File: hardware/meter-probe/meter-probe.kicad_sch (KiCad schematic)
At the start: 37 parts, among them J1 Cable, J2 Cable, SW1 Sensor Button, U1 TSL2585, U2 M24C02-D, U3 PCA9527, U4 TC1301A-APA, U5 USBLC6-2SC6

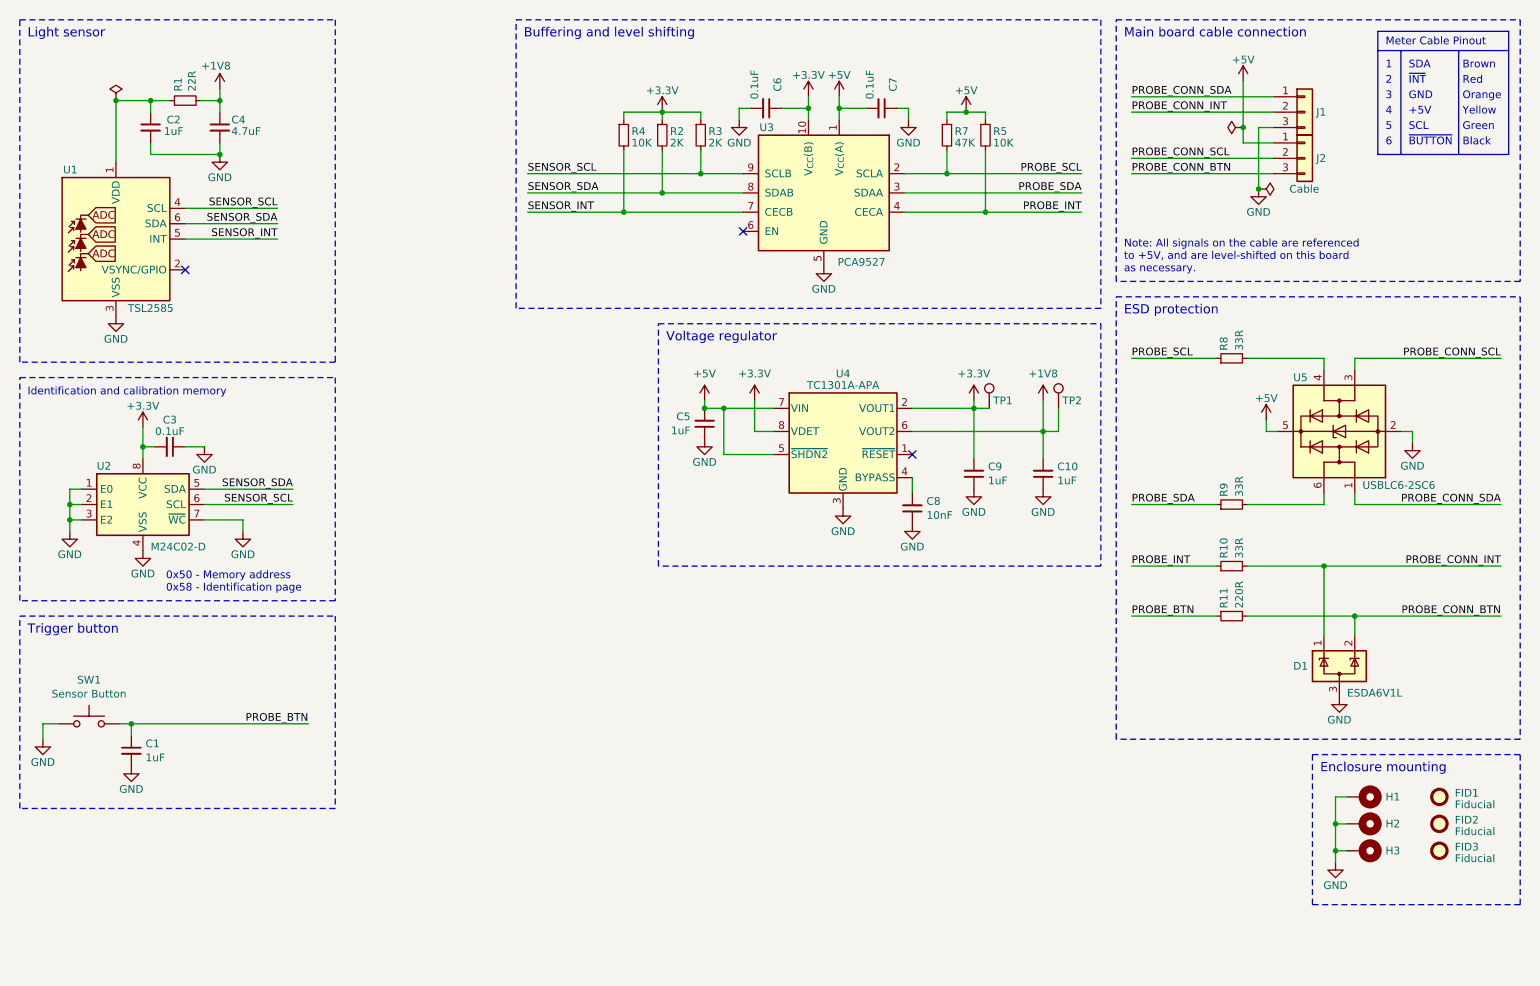
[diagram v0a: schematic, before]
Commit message: Update meter probe with a variety of changes based on testing and eval
- Add a TCA9801 I2C buffer to remove the static offset induced by the
  PCA9527 and provide a clean 1.8V I2C signal to the sensor.
  While the board does work fine without this, the 0.5V static offset
  from the PCA9527 is too close for comfort to the sensor's 0.54V low
  level. So this is a proactive change to reduce potential issues later.
- Add a small series resistor to the push button, to limit the current
  across the debounce capacitor when the button is pressed.
- Add a series of test points at the board edge, so a pogo pin test clip
  can be used more easily to verify board operation prior to attachment
  of the interfae cable.
- Increase board length by 1mm to accomodate the test points.
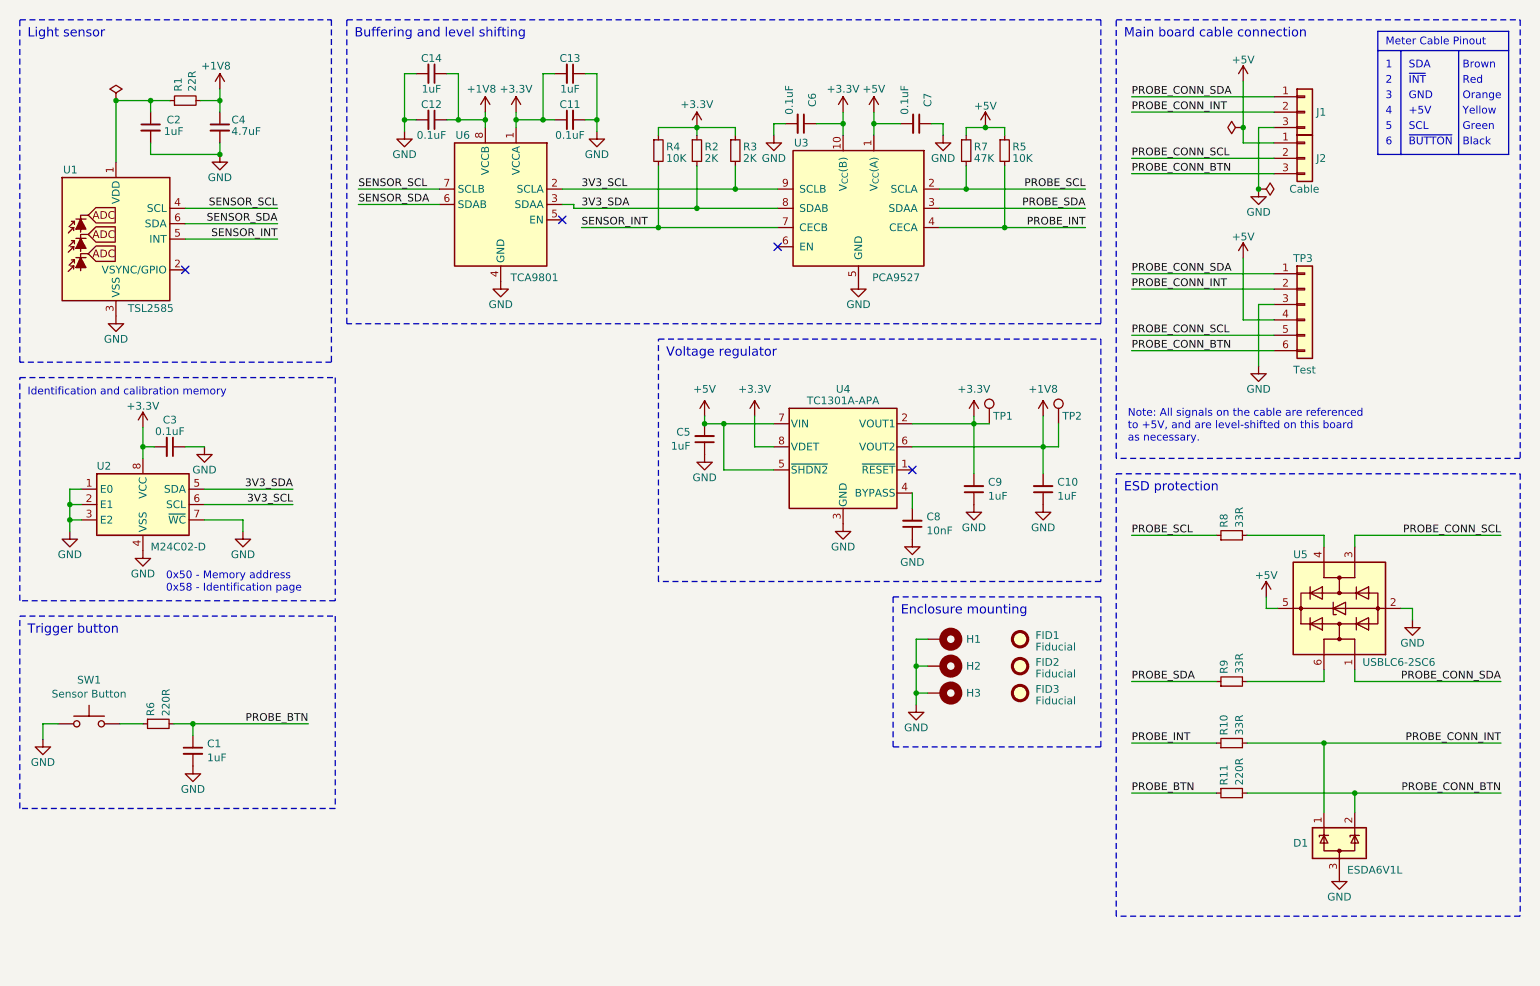
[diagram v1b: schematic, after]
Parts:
- added C11, C12: 0.1uF, Capacitor_SMD:C_0603_1608Metric, symbol Device:C_Small
- added C13, C14: 1uF, Capacitor_SMD:C_0603_1608Metric, symbol Device:C_Small
- added R6: 220R, Resistor_SMD:R_0603_1608Metric, symbol Device:R_Small
- added TP3: Test, lib_fp:TestPoint_1x06_P2.54mm, symbol Connector_Generic:Conn_01x06
- added U6: TCA9801, Package_SO:VSSOP-8_3.0x3.0mm_P0.65mm, symbol Interface:TCA9801
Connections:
- net +1V8: now also C12.1, C14.1, U6.8 (VCCB)
- net +3.3V: now also C11.1, C13.2, U6.1 (VCCA)
- net +5V: now also TP3.4 (Pin_4)
- net GND: now also C11.2, C12.2, C13.1, C14.2, TP3.3 (Pin_3), U6.4 (GND)
- net PROBE_BTN: now also R6.2; no longer SW1.2
- net PROBE_CONN_BTN: now also TP3.6 (Pin_6)
- net PROBE_CONN_INT: now also TP3.2 (Pin_2)
- net PROBE_CONN_SCL: now also TP3.5 (Pin_5)
- net PROBE_CONN_SDA: now also TP3.1 (Pin_1)
- net SENSOR_SCL: now also U6.7 (SCLB); no longer R3.2, U2.6 (SCL), U3.9 (SCLB)
- net SENSOR_SDA: now also U6.6 (SDAB); no longer R2.2, U2.5 (SDA), U3.8 (SDAB)
- new net: R6.1, SW1.2
- new net 3V3_SCL: R3.2, U2.6 (SCL), U3.9 (SCLB), U6.2 (SCLA)
- new net 3V3_SDA: R2.2, U2.5 (SDA), U3.8 (SDAB), U6.3 (SDAA)
- no-connect marks 3 -> 4
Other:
- moved on the sheet: C1, C10, C5, C6, C7, C8, C9, D1, FID1, FID2, FID3, H1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

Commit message: Initial implementation of FT260 in meter probe schematic
This is a big change towards using a USB interface for the meter probe,
and is the first step of getting the schematic portion put together.
Most of the designators will likely change after the layout is started.

The intent of this change is to leverage off-the-shelf mass produced mouse
cables for the physical connection, and to run the meter probe over a
protocol better suited to hot-plugging and noise immunity.
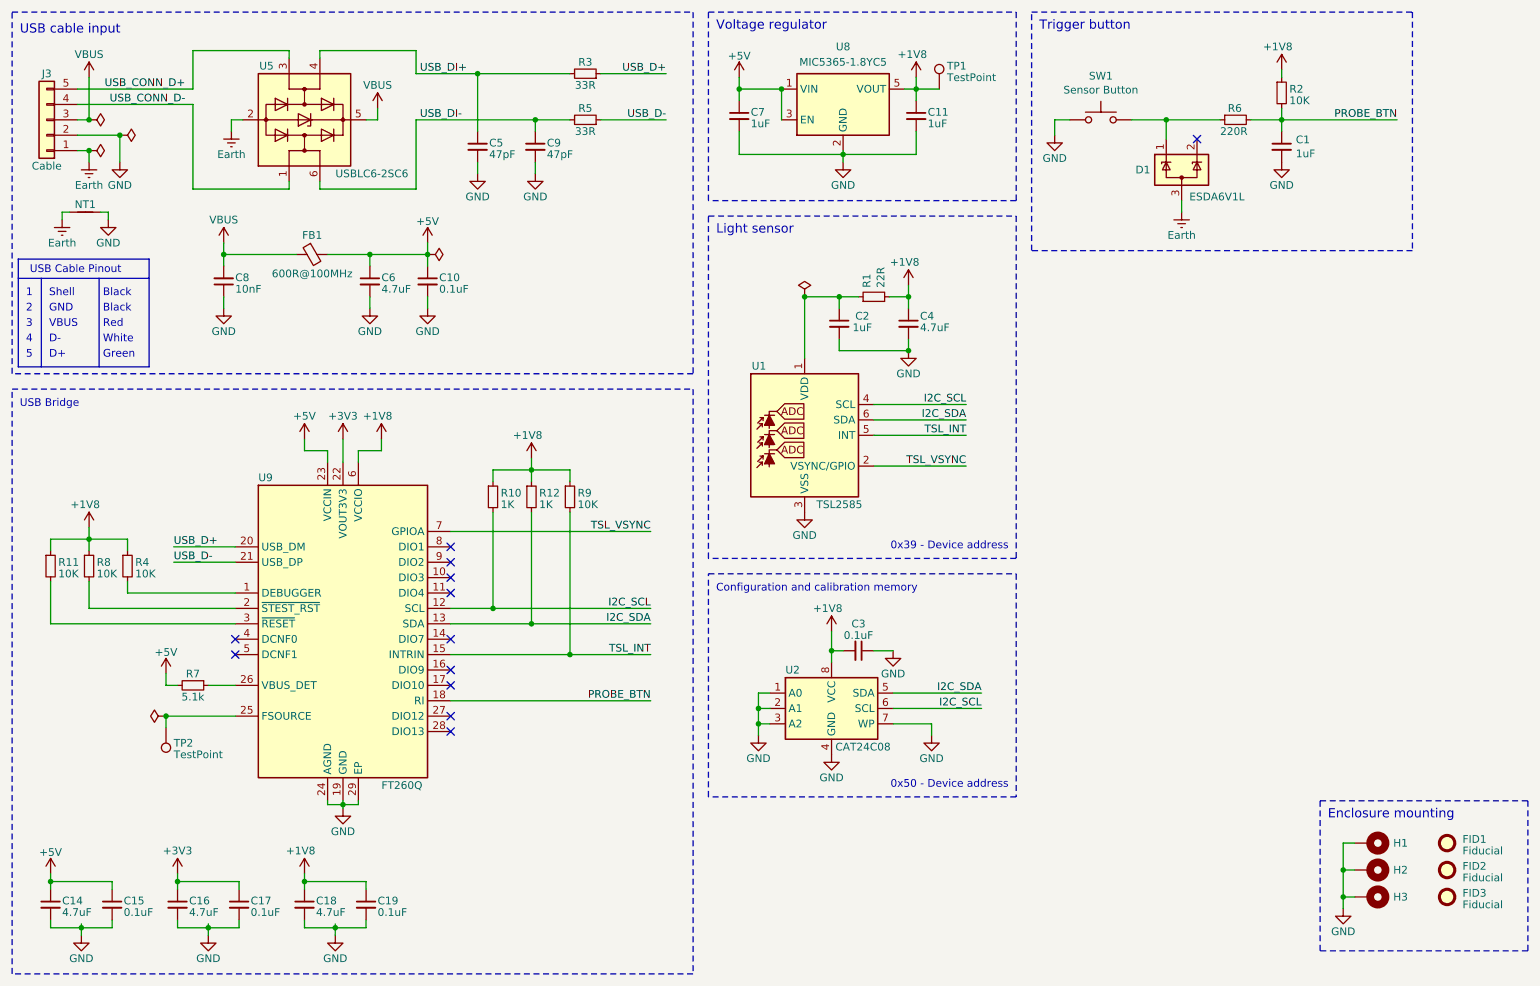
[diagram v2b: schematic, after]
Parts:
- removed C12: 0.1uF, Capacitor_SMD:C_0603_1608Metric, symbol Device:C_Small
- removed C13: 1uF, Capacitor_SMD:C_0603_1608Metric, symbol Device:C_Small
- removed J1, J2: Cable, lib_fp:AVX_IDC-009175-003-001, symbol Connector_Generic:Conn_01x03
- removed TP3: Test, lib_fp:TestPoint_1x06_P2.54mm, symbol Connector_Generic:Conn_01x06
- removed U2: M24C02-D, Package_SO:TSSOP-8_4.4x3mm_P0.65mm, symbol Memory_EEPROM:M24C02-RDW
- removed U3: PCA9527, Package_SO:TSSOP-10_3x3mm_P0.5mm, symbol Project:PCA9527
- removed U4: TC1301A-APA, Package_SO:MSOP-8_3x3mm_P0.65mm, symbol Project:TC1301A
- removed U6: TCA9801, Package_SO:VSSOP-8_3.0x3.0mm_P0.65mm, symbol Interface:TCA9801
- added C15, C17, C19: 0.1uF, Capacitor_SMD:C_0603_1608Metric, symbol Device:C_Small
- added C16, C18: 4.7uF, Capacitor_SMD:C_0603_1608Metric, symbol Device:C_Small
- added FB1: 600R@100MHz, Inductor_SMD:L_0603_1608Metric, symbol Device:FerriteBead_Small
- added J3: Cable, Connector_JST:JST_PH_B5B-PH-SM4-TB_1x05-1MP_P2.00mm_Vertical, symbol Connector_Generic:Conn_01x05
- added NT1: NetTie_2, NetTie:NetTie-2_SMD_Pad0.5mm, symbol Device:NetTie_2
- added R12: 1K, Resistor_SMD:R_0603_1608Metric, symbol Device:R_Small
- added U2: CAT24C08, Package_SO:SOIC-8_3.9x4.9mm_P1.27mm, symbol Project:CAT24C08
- added U8: MIC5365-1.8YC5, Package_TO_SOT_SMD:SOT-353_SC-70-5, symbol Regulator_Linear:MIC5365-3.3YC5
- added U9: FT260Q, lib_fp:FTDI_WQFN-28-1EP_5x5mm_P0.5mm_EP3.3x3.3mm, symbol Project:FT260Q
- C1: Supplier Digi-Key -> LCSC; Supplier PN 1276-1184-1-ND -> C29936
- C10: value 1uF -> 0.1uF; Manufacturer PN CL10B105KA8NNNC -> CL10B104KA8NNNC; Supplier LCSC -> Digi-Key; Supplier PN C29936 -> 1276-1006-1-ND
- C11, C7: value 0.1uF -> 1uF; Manufacturer PN CL10B104KA8NNNC -> CL10B105KA8NNNC; Supplier Digi-Key -> LCSC; Supplier PN 1276-1006-1-ND -> C29936
- C14: value 1uF -> 4.7uF; Manufacturer PN CL10B105KA8NNNC -> CL10A475KA8NQNC; Supplier PN C29936 -> C69335
- C5, C9: value 1uF -> 47pF; Manufacturer Samsung Electro-Mechanics -> YAGEO; Manufacturer PN CL10B105KA8NNNC -> CC0603JRNPO9BN470; Supplier LCSC -> Digi-Key; Supplier PN C29936 -> 311-1065-1-ND
- C6: value 0.1uF -> 4.7uF; Manufacturer PN CL10B104KA8NNNC -> CL10A475KA8NQNC; Supplier Digi-Key -> LCSC; Supplier PN 1276-1006-1-ND -> C69335
- C8: footprint Capacitor_SMD:C_0805_2012Metric -> Capacitor_SMD:C_0603_1608Metric; Manufacturer Samsung Electro-Mechanic -> YAGEO; Manufacturer PN CL21B103KBANNNC -> CC0603KRX7R8BB103; Supplier PN 1276-1015-1-ND -> 311-1360-1-ND
- R10: value 33R -> 1K; Manufacturer YAGEO -> Vishay Dale; Manufacturer PN RC0603JR-0733RL -> CRCW06031K00JNEA; Supplier PN 311-33GRCT-ND -> 541-1.0KGCT-ND
- R11: value 220R -> 10K; Manufacturer YAGEO -> Vishay Dale; Manufacturer PN RC0603JR-07220RL -> CRCW060310K0JNEA; Supplier PN 311-220GRCT-ND -> 541-10KGCT-ND
- R2: value 2K -> 10K; Manufacturer PN CRCW06032K00JNEA -> CRCW060310K0JNEA; Supplier PN 541-2.0KGCT-ND -> 541-10KGCT-ND
- R3: value 2K -> 33R; Manufacturer Vishay Dale -> YAGEO; Manufacturer PN CRCW06032K00JNEA -> RC0603JR-0733RL; Supplier PN 541-2.0KGCT-ND -> 311-33GRCT-ND
- R5: value 10K -> 33R; Manufacturer Vishay Dale -> YAGEO; Manufacturer PN CRCW060310K0JNEA -> RC0603JR-0733RL; Supplier PN 541-10KGCT-ND -> 311-33GRCT-ND
- R7: value 47K -> 5.1k; Manufacturer Vishay Dale -> Yaego; Manufacturer PN CRCW060347K0JNEA -> RC0603JR-075K1L; Supplier Digi-Key -> LCSC; Supplier PN 541-47KGCT-ND -> C14677
- R8, R9: value 33R -> 10K; Manufacturer YAGEO -> Vishay Dale; Manufacturer PN RC0603JR-0733RL -> CRCW060310K0JNEA; Supplier PN 311-33GRCT-ND -> 541-10KGCT-ND
- TP1: value 3.3V -> TestPoint; footprint TestPoint:TestPoint_Pad_D2.0mm -> TestPoint:TestPoint_Pad_D1.0mm; User Label 3.3V -> (none)
- TP2: value 1.8V -> TestPoint; footprint TestPoint:TestPoint_Pad_D2.0mm -> TestPoint:TestPoint_Pad_D1.0mm; User Label 3.3V -> (none)
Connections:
- net 3V3_SDA is gone; now on net PROBE_BTN: R2.2
- net PROBE_SDA is gone; now on net +1V8: R9.1
- net SENSOR_SCL is gone; now on net I2C_SCL: U1.4 (SCL)
- net +1V8: now also C11.1, C3.2, R10.1, R11.1, R2.1, R4.1, R8.1, TP1.1, C18.1, C19.1, R12.1, U2.8 (VCC), U8.5 (VOUT), U9.6 (VCCIO); no longer C10.2, C14.1, TP2.1
- net +5V: now also C10.1, C14.1, C6.1, C7.1, R7.2, C15.1, FB1.2, U8.1 (VIN), U8.3 (EN), U9.23 (VCCIN); no longer C5.2, C7.2, R5.1, R7.1, U5.5 (VBUS)
- net GND: now also C10.2, C5.2, C7.2, C9.2, C15.2, C16.2, C17.2, C18.2, C19.2, J3.2 (Pin_2), NT1.1, U2.1 (A0), U2.2 (A1), U2.3 (A2), U2.4 (GND), U2.7 (WP), U8.2 (GND), U9.19 (GND), U9.24 (AGND), U9.29 (EP); no longer C10.1, C5.1, C7.1, C9.1, D1.3 (A), U5.2 (GND)
- net PROBE_BTN: now also U9.18 (DIO11); no longer R11.1
- net at R6.1, SW1.2: now also D1.1 (K)
- net at R8.2: now also U9.2 (~{STEST_RST}); no longer U5.4 (I/O2)
- net TSL_INT: now reaches R9.2
- net TSL_INT: now also U1.5 (INT), U9.15 (DIO8); no longer U5.6 (I/O1)
- net VBUS: now reaches C8.2
- net VBUS: now also U5.5 (VBUS), FB1.1, J3.3 (Pin_3)
- net TSL_VSYNC: now reaches U1.2 (VSYNC/GPIO)
- net TSL_VSYNC: now also U9.7 (DIO0)
- removed net +3.3V: C11.1, C3.2, C6.1, C9.2, R2.1, R3.1, R4.1, TP1.1
- net 3V3_SCL renamed USB_DI+
- net USB_DI+: now also C5.1, U5.4 (I/O2)
- net PROBE_CONN_BTN: no longer names the net of R11.2
- net PROBE_CONN_BTN: now also U9.3 (~{RESET}); no longer D1.2 (K)
- net PROBE_CONN_INT renamed I2C_SCL
- net I2C_SCL: now also U2.6 (SCL), U9.12 (DIO5); no longer D1.1 (K)
- net PROBE_CONN_SCL renamed USB_CONN_D+
- net USB_CONN_D+: now also J3.5 (Pin_5)
- net PROBE_CONN_SDA renamed USB_CONN_D-
- net USB_CONN_D-: now also J3.4 (Pin_4)
- net PROBE_INT renamed USB_DI-
- net USB_DI-: now also C9.1, U5.6 (I/O1); no longer R10.1
- removed net PROBE_SCL: R7.2, R8.1
- net SENSOR_INT: no longer names the net of R4.2
- net SENSOR_INT: now also U9.1 (DEBUGGER); no longer U1.5 (INT)
- net SENSOR_SDA renamed I2C_SDA
- net I2C_SDA: now also R12.2, U2.5 (SDA), U9.13 (DIO6)
- new net: TP2.1, U9.25 (FSOURCE)
- new net: R7.1, U9.26 (VBUS_DET)
- new net +3V3: C16.1, C17.1, U9.22 (VOUT3V3)
- new net Earth: D1.3 (A), J3.1 (Pin_1), NT1.2, U5.2 (GND)
- new net USB_D+: R3.1, U9.20 (USB_DM)
- new net USB_D-: R5.1, U9.21 (USB_DP)
- no-connect marks 4 -> 12
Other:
- note added: "0x39 - Device address"
- note added: "0x50 - Device address"
- note added: "Configuration and calibration memory"
- note added: "D+"
- note added: "D-"
- note added: "Shell"
- note added: "USB Bridge"
- note added: "USB Cable Pinout"
- note added: "USB cable input"
- note added: "VBUS"
- note added: "White"
- note removed: "+5V"
- note removed: "0x50 - Memory address 0x58 - Identification page"
- note removed: "6"
- note removed: "Brown"
- note removed: "Buffering and level shifting"
- note removed: "ESD protection"
- note removed: "Identification and calibration memory"
- note removed: "Main board cable connection"
- note removed: "Meter Cable Pinout"
- note removed: "Note: All signals on the cable are referenced to +5V, and are level-shifted on this board as necessary."
- note removed: "Orange"
- note removed: "SCL"
- note removed: "SDA"
- note removed: "Yellow"
- note removed: "~{BUTTON}"
- note removed: "~{INT}"
- moved on the sheet: C1, C2, C3, C4, C8, D1, FID1, FID2, FID3, H1, H2, H3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

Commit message: Initial layout for USB meter probe design
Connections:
- net USB_CONN_D+: now also U5.1 (I/O1); no longer U5.3 (I/O2)
- net USB_CONN_D-: now also U5.3 (I/O2); no longer U5.1 (I/O1)
- net USB_DI+: now also U5.6 (I/O1); no longer U5.4 (I/O2)
- net USB_DI-: now also U5.4 (I/O2); no longer U5.6 (I/O1)
- net at R6.1, SW1.2: now also D1.2 (K); no longer D1.1 (K)
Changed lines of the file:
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@@
   (junction (at 27.305 32.385) (diameter 0) (color 0 0 0 0)
   )
+  (junction (at 210.185 32.385) (diameter 0) (color 0 0 0 0)
+  )
   (junction (at 69.215 145.415) (diameter 0) (color 0 0 0 0)
   )
@@
   )
   (junction (at 134.62 27.305) (diameter 0) (color 0 0 0 0)
-  )
-  (junction (at 205.105 32.385) (diameter 0) (color 0 0 0 0)
   )
   (junction (at 41.91 158.115) (diameter 0) (color 0 0 0 0)
@@
   (no_connect (at 86.995 110.49))
   (no_connect (at 86.995 105.41))
-  (no_connect (at 210.185 35.56))
+  (no_connect (at 205.105 35.56))
   (no_connect (at 86.995 102.87))
   (no_connect (at 51.435 120.65))
@@
     (stroke (width 0) (type default))
   )
+  (wire (pts (xy 210.185 32.385) (xy 213.995 32.385))
+    (stroke (width 0) (type default))
+  )
   (wire (pts (xy 62.865 158.115) (xy 73.025 158.115))
     (stroke (width 0) (type default))
@@
     (stroke (width 0) (type default))
   )
-  (wire (pts (xy 205.105 32.385) (xy 205.105 35.56))
-    (stroke (width 0) (type default))
-  )
   (wire (pts (xy 73.66 54.61) (xy 83.185 54.61))
     (stroke (width 0) (type default))
@@
     (stroke (width 0) (type default))
   )
-  (wire (pts (xy 199.39 32.385) (xy 205.105 32.385))
+  (wire (pts (xy 199.39 32.385) (xy 210.185 32.385))
     (stroke (width 0) (type default))
   )
@@
     (stroke (width 0) (type default))
   )
-  (wire (pts (xy 205.105 32.385) (xy 213.995 32.385))
-    (stroke (width 0) (type default))
-  )
   (wire (pts (xy 162.56 59.69) (xy 162.56 61.595))
     (stroke (width 0) (type default))
@@
   )
   (wire (pts (xy 141.605 27.305) (xy 141.605 32.385))
+    (stroke (width 0) (type default))
+  )
+  (wire (pts (xy 210.185 32.385) (xy 210.185 35.56))
     (stroke (width 0) (type default))
   )
@@
     )
   )
-  (symbol (lib_id "Power_Protection:USBLC6-2SC6") (at 62.865 32.385 270) (mirror x) (unit 1)
-    (in_bom yes) (on_board yes) (dnp no)
-    (property "Reference" "U5" (at 57.785 23.495 90)
-      (effects (font (size 1.27 1.27)) (justify right))
-    )
-    (property "Value" "USBLC6-2SC6" (at 80.01 41.275 90)
-      (effects (font (size 1.27 1.27)) (justify right))
+  (symbol (lib_id "Power_Protection:USBLC6-2SC6") (at 62.865 32.385 270) (unit 1)
+    (in_bom yes) (on_board yes) (dnp no)
+    (property "Reference" "U5" (at 55.245 23.495 90)
+      (effects (font (size 1.27 1.27)) (justify left))
+    )
+    (property "Value" "USBLC6-2SC6" (at 66.04 41.275 90)
+      (effects (font (size 1.27 1.27)) (justify left))
     )
     (property "Footprint" "Package_TO_SOT_SMD:SOT-23-6" (at 50.165 32.385 0)
       (effects (font (size 1.27 1.27)) hide)
     )
-    (property "Datasheet" "https://www.st.com/resource/en/datasheet/usblc6-2.pdf" (at 71.755 27.305 0)
-      (effects (font (size 1.27 1.27)) hide)
-    )
+    (property "Datasheet" "https://www.st.com/resource/en/datasheet/usblc6-2.pdf" (at 71.755 37.465 0)
+      (effects (font (size 1.27 1.27)) hide)
+    )

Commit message: Clean up reference designators
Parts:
- renumbered C2 to C1, C14 to C10, C15 to C11, C16 to C12, C17 to C13, C18 to C14, C19 to C15, C3 to C16, C1 to C17, C4 to C2, C5 to C3, C9 to C4, C8 to C5, C10 to C7, C7 to C8, C11 to C9, J3 to J1, R7 to R10, R2 to R11, R6 to R12, R3 to R2, R5 to R3, R10 to R4, R12 to R5, R9 to R6, R11 to R7, R4 to R9, U5 to U2, U8 to U3, U9 to U4, U2 to U5

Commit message: Meter probe changes from lab testing
Added pull-down resistor to DCD to prevent unwanted interrupts,
since it is enabled as part of enabling DI.

Added a series resistor and test point for the GPIOA pin that
is routed to VSYNC.

Various minor layout tweaks
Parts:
- added R13: 33R, Resistor_SMD:R_0603_1608Metric, symbol Device:R_Small
- added TP3: TestPoint, TestPoint:TestPoint_Pad_D1.0mm, symbol Connector:TestPoint
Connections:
- net GND: now also U4.17 (DIO10)
- net TSL_VSYNC: now also R13.1, TP3.1; no longer U4.7 (DIO0)
- net at R12.1, SW1.2: now also D1.1 (K); no longer D1.2 (K)
- new net: R13.2, U4.7 (DIO0)
- no-connect marks 12 -> 11
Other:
- note added: "DCFN0 and DCFN1 have internal pull-downs DCD is held low to avoid spurious interrupts GPIOA has a series resistor to reduce slew rate"
- moved on the sheet: R4, R5, R6, TP2
